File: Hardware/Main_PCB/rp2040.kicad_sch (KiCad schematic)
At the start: 30 parts, among them P301 USB_C_Plug_USB2.0, SW301 Reset button, SW302 TL3342F160QG_TR, U301 RP2040, U302 W25Q128JVS, Y301 12Mhz

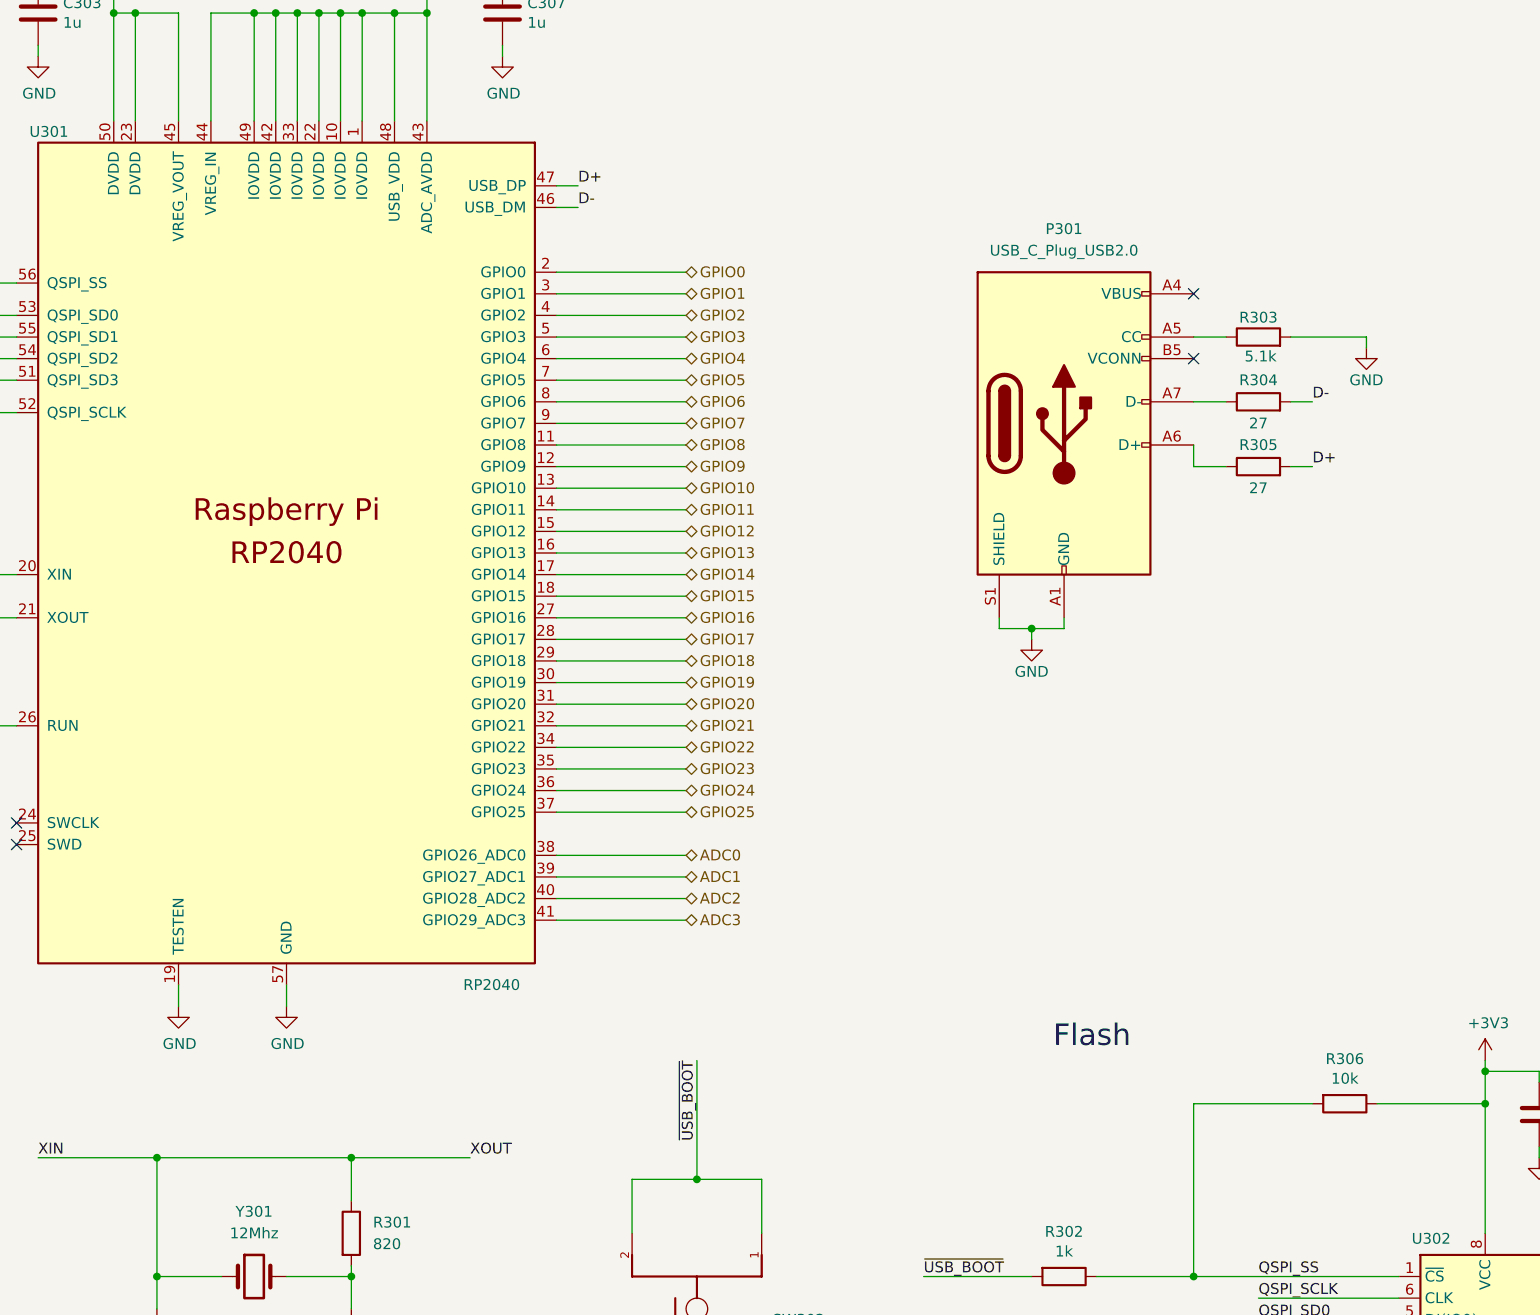
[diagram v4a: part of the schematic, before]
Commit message: Added footprints to all components
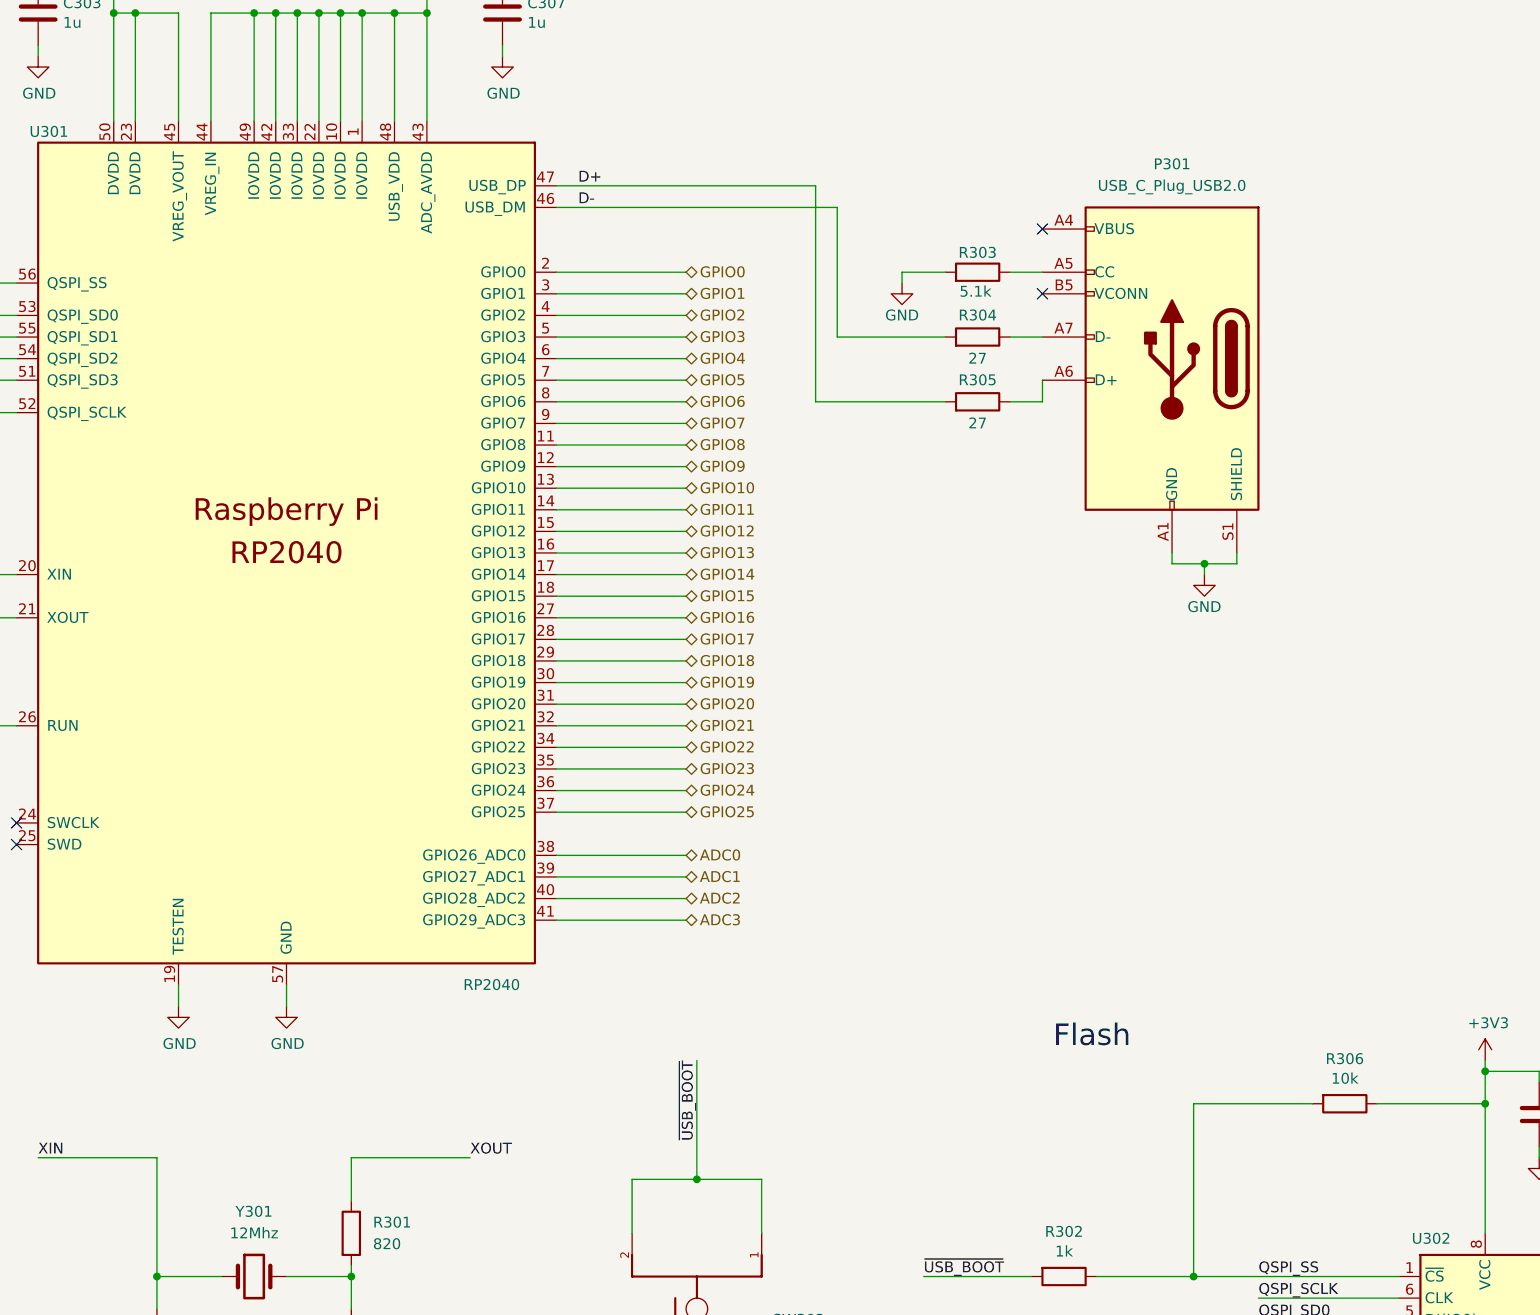
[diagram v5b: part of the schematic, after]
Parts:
- P301: footprint (none) -> Connector_USB:USB_C_Receptacle_Molex_105450-0101
- R301, R303, R304, R305: footprint (none) -> Resistor_SMD:R_0603_1608Metric_Pad0.98x0.95mm_HandSolder
- SW301: footprint (none) -> Button_Switch_SMD:SW_SPST_B3U-1000P
- SW302: footprint TL3342F160QG_TR:SW_TL3342F160QG_TR -> MainPCB:SW_TL3342F160QG_TR
- U301: footprint RP2040_minimal:RP2040-QFN-56 -> Package_DFN_QFN:QFN-56-1EP_7x7mm_P0.4mm_EP3.2x3.2mm
- U302: footprint Package_SO:SOIC-8_5.23x5.23mm_P1.27mm -> Package_SO:SOIC-8_5.3x5.3mm_P1.27mm
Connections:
- net XIN: no longer R301.1, U301.21 (XOUT)
- new net XOUT: R301.1, U301.21 (XOUT)
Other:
- moved on the sheet: P301, R303, R304, R305

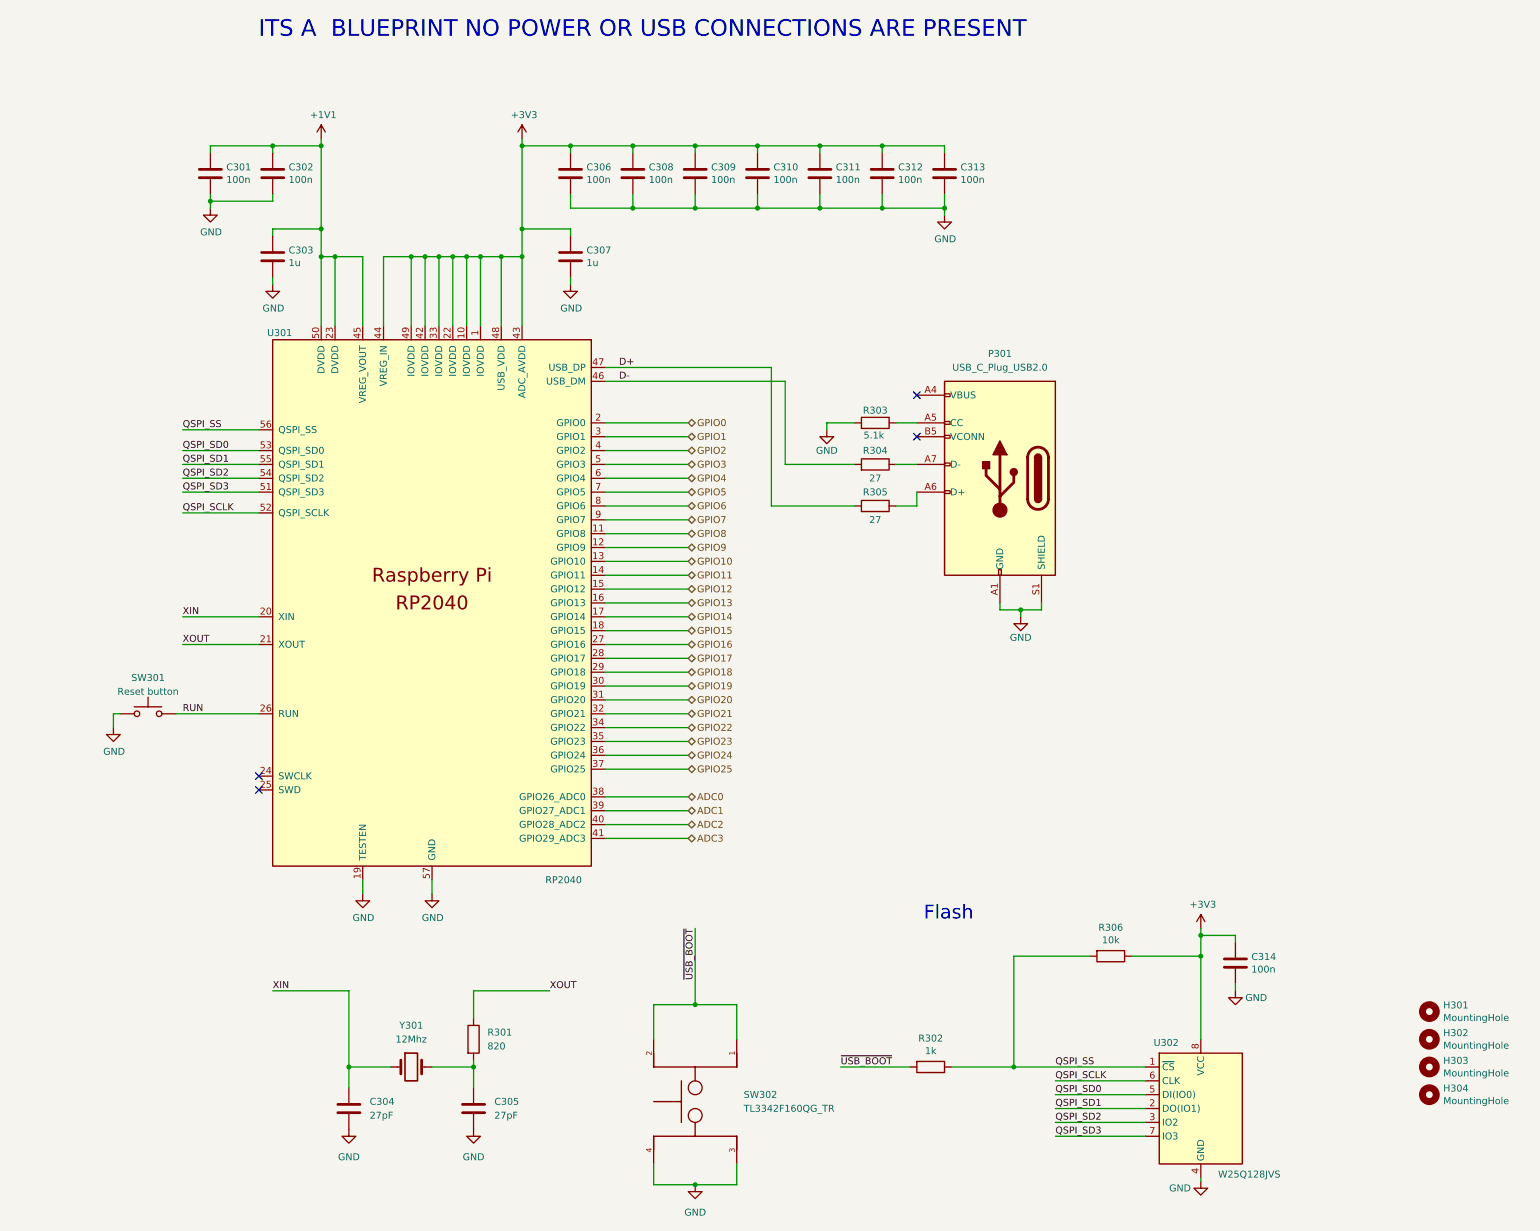
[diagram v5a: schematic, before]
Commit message: Finished the schematic of the MainPCB
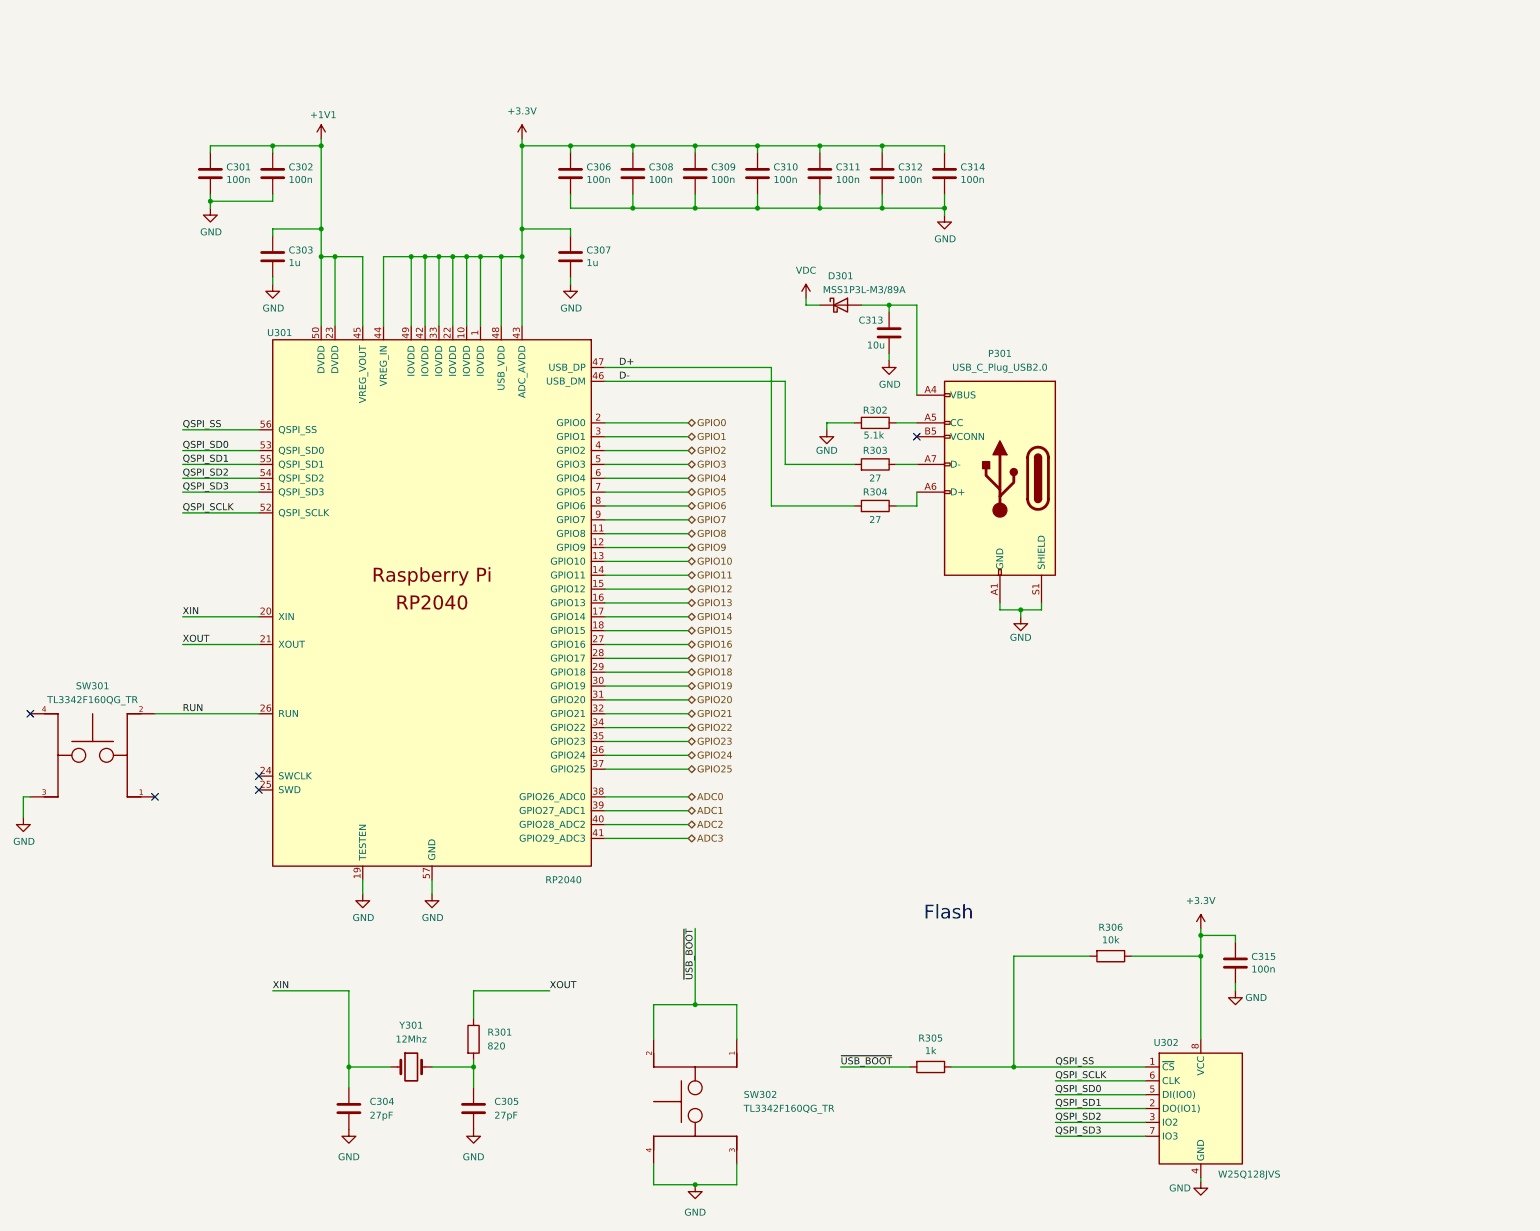
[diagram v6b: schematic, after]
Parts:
- removed H301, H302, H303, H304: MountingHole, MountingHole:MountingHole_2.7mm_M2.5, symbol Mechanical:MountingHole
- removed SW301: Reset button, Button_Switch_SMD:SW_SPST_B3U-1000P, symbol Switch:SW_Push
- added C313: 10u, Capacitor_SMD:C_0603_1608Metric_Pad1.08x0.95mm_HandSolder, symbol Device:C
- added D301: MSS1P3L-M3/89A, Diode_SMD:Vishay_SMPA, symbol Device:D_Schottky
- added SW301: TL3342F160QG_TR, MainPCB:SW_TL3342F160QG_TR, symbol TL3342F160QG_TR:TL3342F160QG_TR
- R305: renamed from R302; footprint Resistor_SMD:R_0402_1005Metric -> Resistor_SMD:R_0603_1608Metric_Pad0.98x0.95mm_HandSolder
- R306: footprint Resistor_SMD:R_0402_1005Metric -> Resistor_SMD:R_0603_1608Metric_Pad0.98x0.95mm_HandSolder
- renumbered C313 to C314, C314 to C315, R303 to R302, R304 to R303, R305 to R304
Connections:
- net GND: now also C313.2, SW301.3
- net RUN: now also SW301.2
- net at P301.A4 (VBUS), P301.A9 (VBUS), P301.B4 (VBUS)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: now also C313.1, D301.2 (A)
- net +3V3 renamed +3.3V
- new net VDC: D301.1 (K)
- no-connect marks 4 -> 5
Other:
- note removed: "ITS A BLUEPRINT NO POWER OR USB CONNECTIONS ARE PRESENT"

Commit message: Probably a final version of the MAIN PCB component placement
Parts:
- P301: footprint Connector_USB:USB_C_Receptacle_Molex_105450-0101 -> MainPCB:CUI_UJC-HP-3-SMT-TR
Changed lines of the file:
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@@
 			)
 		)
-		(property "Footprint" "Connector_USB:USB_C_Receptacle_Molex_105450-0101"
+		(property "Footprint" "MainPCB:CUI_UJC-HP-3-SMT-TR"
 			(at 208.28 120.65 0)
 			(effects
